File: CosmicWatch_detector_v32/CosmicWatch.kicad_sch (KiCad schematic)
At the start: 97 parts, among them J3 RJ45, P1 CONN_01X04, P10 CONN_02X02, P11 CONN_01X01, P12 CONN_01X01, P13 CONN_01X01, P14 CONN_01X01, P15 CONN_02X04, P16 CONN_01X02, P19 CONN_01X01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

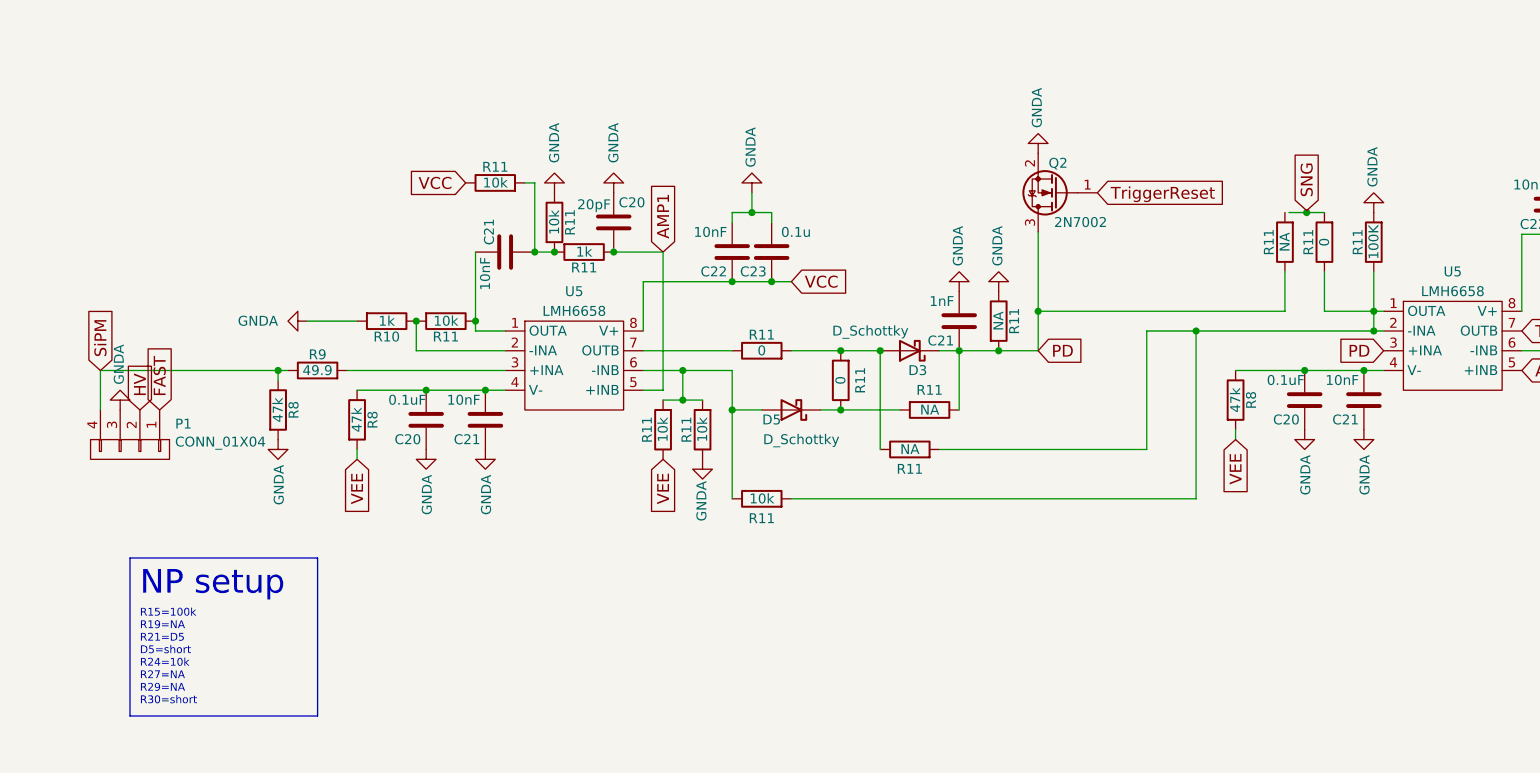
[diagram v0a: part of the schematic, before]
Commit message: updating pcb
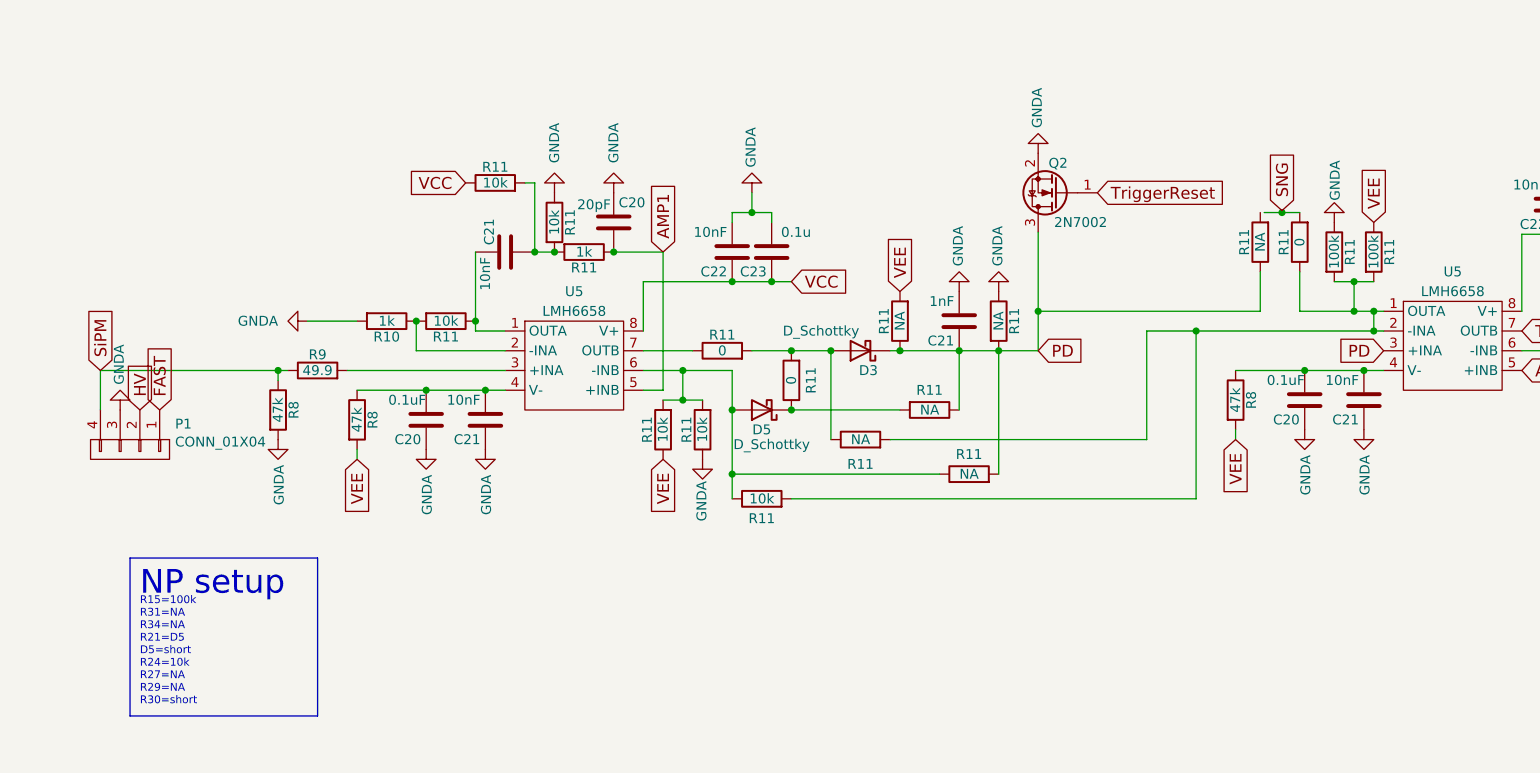
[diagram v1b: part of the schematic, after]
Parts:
- added R11 (x2): 100k, Capacitor_SMD:C_0603_1608Metric, symbol device:R
- added R11: NA, Capacitor_SMD:C_0603_1608Metric, symbol device:R
- R11: value 100K -> NA
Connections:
- net GNDA: now also R11.1; no longer R11.2
- net PD: now also R11.1, R11.2
- net VEE: now also R11.2, R11.1
- net at D5.2 (A), R11.1, R11.2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: now also R11.1
- net at R11.1, R11.2, R11.2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: now also R11.2, R11.2; no longer R11.1
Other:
- note added: "R15=100k R31=NA R34=NA R21=D5 D5=short R24=10k R27=NA R29=NA R30=short"
- note removed: "R15=100k R19=NA R21=D5 D5=short R24=10k R27=NA R29=NA R30=short"
- moved on the sheet: D3, D5, R11
